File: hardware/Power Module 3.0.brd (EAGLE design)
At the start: 99.1 x 69.8 mm, 29 parts, among them IC1 LM358N, J1 AC_IN, J2 To_Relay, J3 From_Relay, J4 AC_OUT, J5 To_Reg, J6 From_Reg, J7 54601-908WPLFW/MODEL, K1 T9AS1D22-54PIN, K2 T9AS1D22-54PIN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

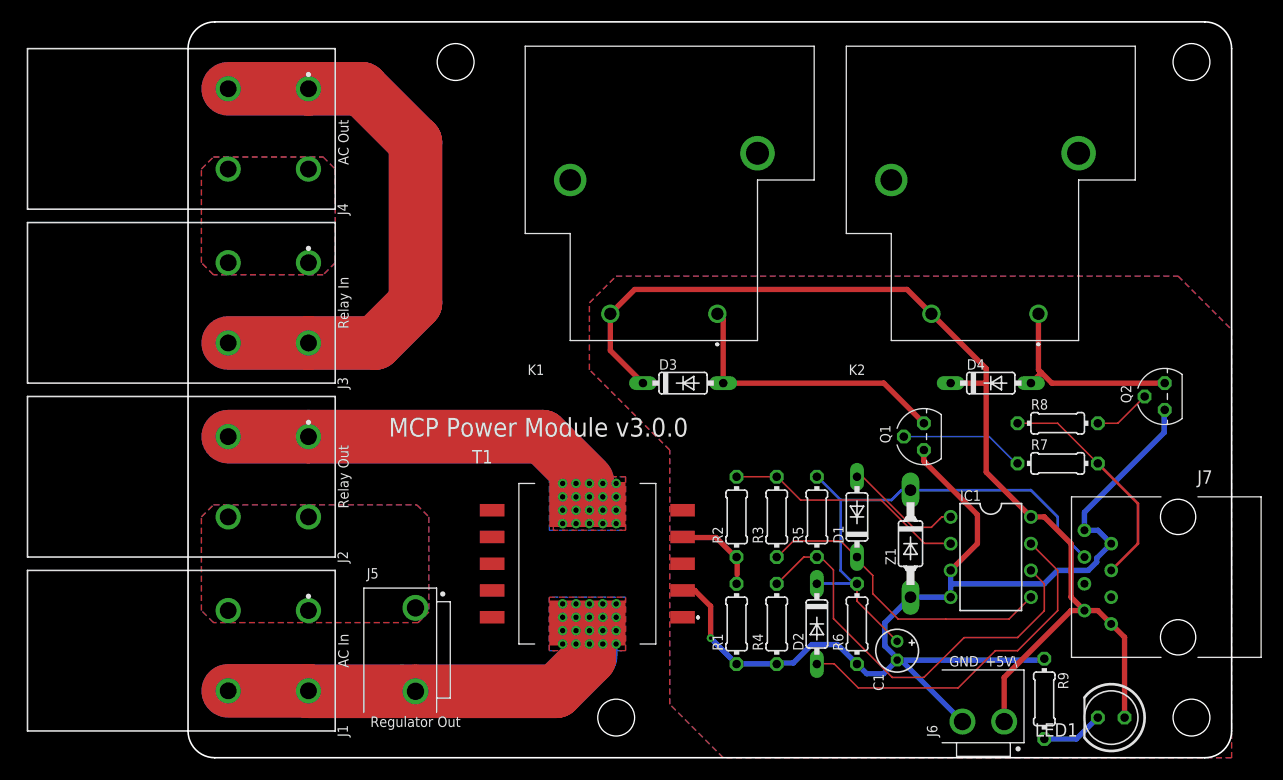
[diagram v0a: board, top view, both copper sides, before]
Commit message: Minor Power Module layout tweaks, rename files
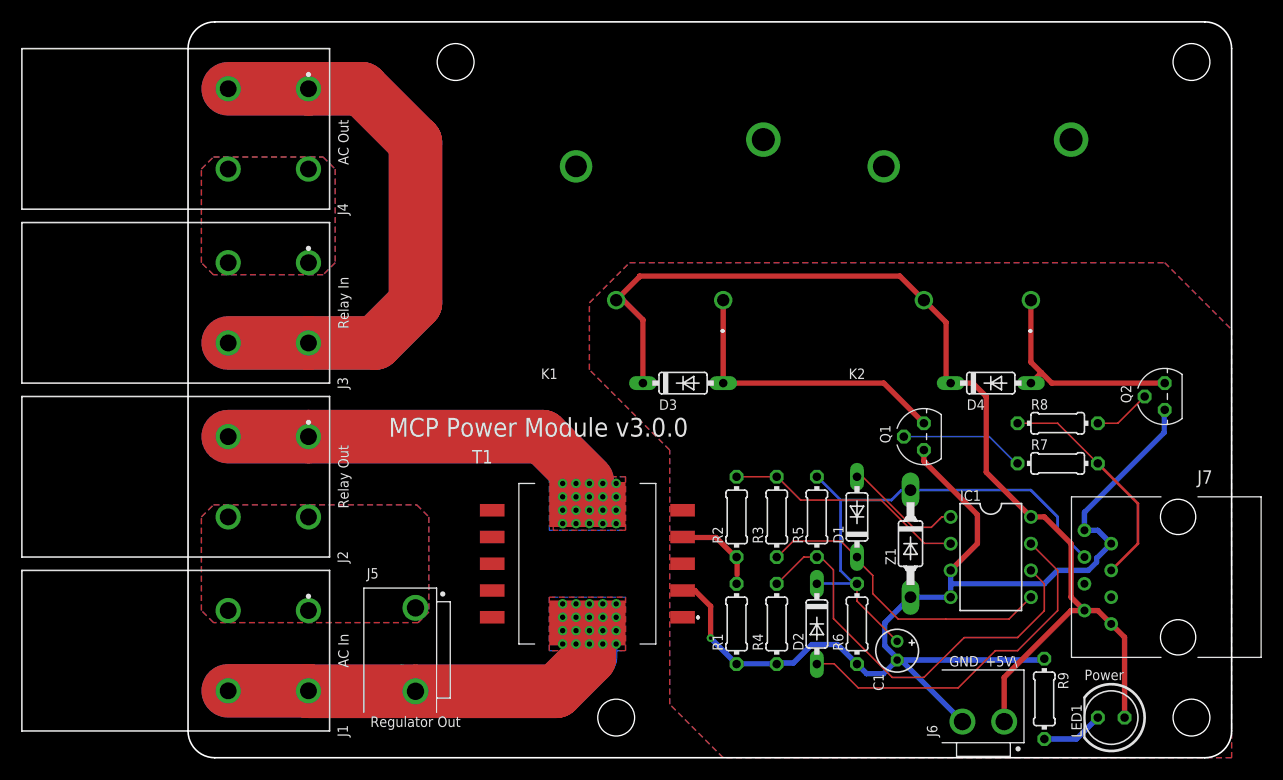
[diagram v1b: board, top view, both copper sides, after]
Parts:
- moved K1 22.5 mm to (61.0, 69.8)
- moved K2 21.6 mm to (90.2, 69.8)
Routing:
- net N$11: track 19.2 -> 20.8 mm
- net N$8: track 27.4 -> 28.5 mm
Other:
- board text added: "Power"
